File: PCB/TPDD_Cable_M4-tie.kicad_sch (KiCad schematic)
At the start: 9 parts, among them J1 TPDD_RS-232C, P3 RX, P4 RTS, P5 CTS, P6 DSR, Q1 DTA114EKA, Q2 DTA114EKA, Q3 DTA114EKA

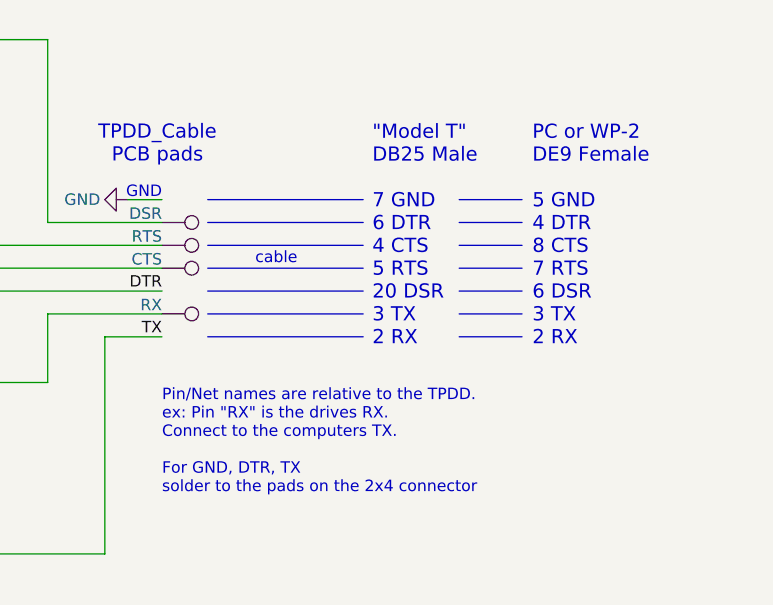
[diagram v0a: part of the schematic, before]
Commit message: schematics notes text
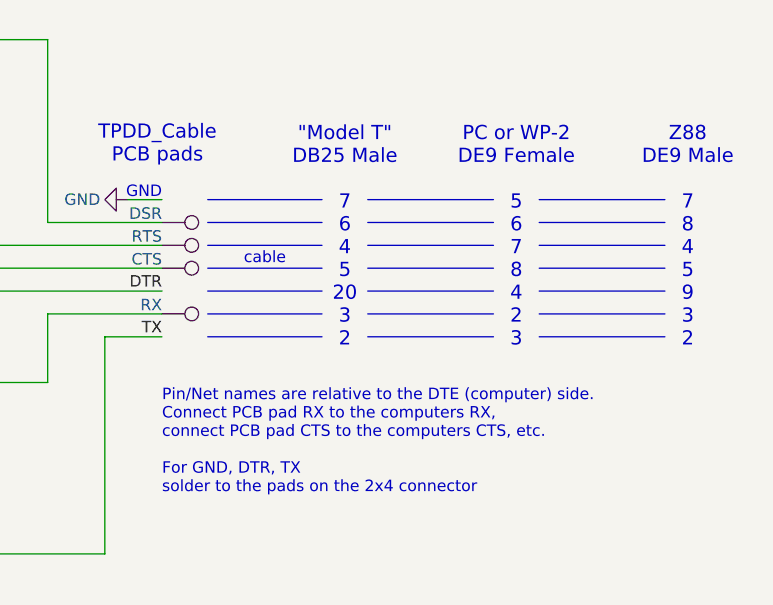
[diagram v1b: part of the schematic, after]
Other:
- note added: ""Model T" DB25 Male 7 6 4 5 20 3 2"
- note added: "PC or WP-2 DE9 Female 5 6 7 8 4 2 3"
- note added: "Pin/Net names are relative to the DTE (computer) side. Connect PCB pad RX to the computers RX, connect PCB pad CTS to the computers CTS, etc. For GND, DTR, TX solder to the pads on the 2x4 connector"
- note added: "Z88 DE9 Male 7 8 4 5 9 3 2"
- note removed: ""Model T" DB25 Male 7 GND 6 DTR 4 CTS 5 RTS 20 DSR 3 TX 2 RX"
- note removed: "PC or WP-2 DE9 Female 5 GND 4 DTR 8 CTS 7 RTS 6 DSR 3 TX 2 RX"
- note removed: "Pin/Net names are relative to the TPDD. ex: Pin "RX" is the drives RX. Connect to the computers TX. For GND, DTR, TX solder to the pads on the 2x4 connector"
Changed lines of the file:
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@@
-		)
-	)
-	(polyline
-		(pts
-			(xy 217.17 83.82) (xy 224.155 83.82)
-		)
-		(stroke
-			(width 0)
-			(type default)
 		)
 	)
@@
 	(polyline
 		(pts
-			(xy 217.17 71.12) (xy 224.155 71.12)
+			(xy 189.23 81.28) (xy 201.93 81.28)
+		)
+		(stroke
+			(width 0)
+			(type default)
+		)
+	)
+	(polyline
+		(pts
+			(xy 189.23 76.2) (xy 201.93 76.2)
+		)
+		(stroke
+			(width 0)
+			(type default)
+		)
+	)
+	(polyline
+		(pts
+			(xy 207.01 81.28) (xy 220.98 81.28)
 		)
 		(stroke
@@
 	(polyline
 		(pts
-			(xy 189.23 83.82) (xy 206.502 83.82)
-		)
-		(stroke
-			(width 0)
-			(type default)
-		)
-	)
-	(polyline
-		(pts
-			(xy 189.23 78.74) (xy 206.502 78.74)
+			(xy 226.06 73.66) (xy 240.03 73.66)
+		)
+		(stroke
+			(width 0)
+			(type default)
+		)
+	)
+	(polyline
+		(pts
+			(xy 207.01 73.66) (xy 220.98 73.66)
+		)
+		(stroke
+			(width 0)
+			(type default)
+		)
+	)
+	(polyline
+		(pts
+			(xy 189.23 68.58) (xy 201.93 68.58)
 		)
 		(stroke
@@
 		)
 	)
+	(polyline
+		(pts
+			(xy 189.23 71.12) (xy 201.93 71.12)
+		)
+		(stroke
+			(width 0)
+			(type default)
+		)
+	)
 	(wire
 		(pts
@@
 	(polyline
 		(pts
-			(xy 189.23 76.2) (xy 206.502 76.2)
-		)
-		(stroke
-			(width 0)
-			(type default)
-		)
-	)
-	(polyline
-		(pts
-			(xy 217.17 68.58) (xy 224.155 68.58)
+			(xy 207.01 71.12) (xy 220.98 71.12)
 		)
 		(stroke
@@
 	(polyline
 		(pts
-			(xy 217.17 78.74) (xy 224.155 78.74)
+			(xy 226.06 83.82) (xy 240.03 83.82)
+		)
+		(stroke
+			(width 0)
+			(type default)
+		)
+	)
+	(polyline
+		(pts
+			(xy 226.06 81.28) (xy 240.03 81.28)
 		)
 		(stroke
@@
 	(polyline
 		(pts
-			(xy 189.23 71.12) (xy 206.502 71.12)
+			(xy 207.01 78.74) (xy 220.98 78.74)
 		)
 		(stroke
@@
 		)
 	)
+	(polyline
+		(pts
+			(xy 207.01 68.58) (xy 220.98 68.58)
+		)
+		(stroke
+			(width 0)
+			(type default)
+		)
+	)
+	(polyline
+		(pts
+			(xy 189.23 78.74) (xy 201.93 78.74)
+		)
+		(stroke
+			(width 0)
+			(type default)
+		)
+	)
 	(wire
 		(pts
@@
 		)
 	)
-	(polyline
-		(pts
-			(xy 189.23 68.58) (xy 206.502 68.58)
-		)
-		(stroke
-			(width 0)
-			(type default)
-		)
-	)
 	(wire
 		(pts
@@
 		)
 	)
+	(polyline
+		(pts
+			(xy 189.23 83.82) (xy 201.93 83.82)
+		)
+		(stroke
+			(width 0)
+			(type default)
+		)
+	)
+	(polyline
+		(pts
+			(xy 189.23 73.66) (xy 201.93 73.66)
+		)
+		(stroke
+			(width 0)
+			(type default)
+		)
+	)
 	(wire
 		(pts
@@
 		)
 	)
+	(polyline
+		(pts
+			(xy 207.01 83.82) (xy 220.98 83.82)
+		)
+		(stroke
+			(width 0)
+			(type default)
+		)
+	)
 	(wire
 		(pts
@@
 		)
 	)
+	(polyline
+		(pts
+			(xy 207.01 76.2) (xy 220.98 76.2)
+		)
+		(stroke
+			(width 0)
+			(type default)
+		)
+	)
 	(wire
 		(pts
@@
 	(polyline
 		(pts
-			(xy 217.17 76.2) (xy 224.155 76.2)
-		)
-		(stroke
-			(width 0)
-			(type default)
-		)
-	)
-	(polyline
-		(pts
-			(xy 217.17 73.66) (xy 224.155 73.66)
+			(xy 226.06 78.74) (xy 240.03 78.74)
 		)
 		(stroke
@@
 	(polyline
 		(pts
-			(xy 217.17 81.28) (xy 224.155 81.28)
-		)
-		(stroke
-			(width 0)
-			(type default)
-		)
-	)
-	(polyline
-		(pts
-			(xy 189.23 81.28) (xy 206.502 81.28)
-		)
-		(stroke
-			(width 0)
-			(type default)
-		)
-	)
-	(polyline
-		(pts
-			(xy 189.23 73.66) (xy 206.502 73.66)
+			(xy 226.06 68.58) (xy 240.03 68.58)
+		)
+		(stroke
+			(width 0)
+			(type default)
+		)
+	)
+	(polyline
+		(pts
+			(xy 226.06 76.2) (xy 240.03 76.2)
 		)
 		(stroke
@@
 		)
 	)
+	(polyline
+		(pts
+			(xy 226.06 71.12) (xy 240.03 71.12)
+		)
+		(stroke
+			(width 0)
+			(type default)
+		)
+	)
 	(text "TPDD_Cable\nPCB pads"
 		(exclude_from_sim no)
@@
 		)
 	)
-	(text "PC or WP-2\nDE9 Female\n\n5 GND\n4 DTR\n8 CTS\n7 RTS\n6 DSR\n3 TX\n2 RX"
-		(exclude_from_sim no)
-		(at 225.298 72.644 0)
+	(text "Z88\nDE9 Male\n\n7\n8\n4\n5\n9\n3\n2"
+		(exclude_from_sim no)
+		(at 242.57 60.452 0)
 		(effects
 			(font
 				(size 1.5748 1.5748)
 			)
-			(justify left)
+			(justify top)
 		)
 	)
@@
 		)
 	)
-	(text "\"Model T\"\nDB25 Male\n\n7 GND\n6 DTR\n4 CTS\n5 RTS\n20 DSR\n3 TX\n2 RX"
-		(exclude_from_sim no)
-		(at 207.518 72.644 0)
+	(text "(1)"
+		(exclude_from_sim no)
+		(at 107.315 80.01 0)
+		(effects
+			(font
+				(size 1.27 1.27)
+			)
+			(justify left bottom)
+		)
+	)
+	(text "\"Model T\"\nDB25 Male\n\n7\n6\n4\n5\n20\n3\n2"
+		(exclude_from_sim no)
+		(at 204.47 60.452 0)
 		(effects
 			(font
 				(size 1.5748 1.5748)
 			)
-			(justify left)
-		)
-	)
-	(text "(1)"
-		(exclude_from_sim no)
-		(at 107.315 80.01 0)
+			(justify top)
+		)
+	)
+	(text "Pin/Net names are relative to the DTE (computer) side.\nConnect PCB pad RX to the computers RX,\nconnect PCB pad CTS to the computers CTS, etc.\n\nFor GND, DTR, TX\nsolder to the pads on the 2x4 connector\n"
+		(exclude_from_sim no)
+		(at 184.15 89.662 0)
 		(effects
 			(font
 				(size 1.27 1.27)
 			)
-			(justify left bottom)
+			(justify left top)
 		)
 	)
 	(text "cable"
 		(exclude_from_sim no)
-		(at 196.85 75.184 0)
+		(at 195.58 75.184 0)
 		(effects
 			(font
@@
 		)
 	)
-	(text "Pin/Net names are relative to the TPDD.\nex: Pin \"RX\" is the drives RX.\nConnect to the computers TX.\n\nFor GND, DTR, TX\nsolder to the pads on the 2x4 connector\n"
-		(exclude_from_sim no)
-		(at 184.15 89.662 0)
-		(effects
-			(font
-				(size 1.27 1.27)
-			)
-			(justify left top)
-		)
-	)
+	(text "PC or WP-2\nDE9 Female\n\n5\n6\n7\n8\n4\n2\n3"
+		(exclude_from_sim no)
+		(at 223.52 60.452 0)
+		(effects
+			(font
+				(size 1.5748 1.5748)
+			)
+			(justify top)
+		)
+	)
